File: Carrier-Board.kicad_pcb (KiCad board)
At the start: 4 copper layers, 92 x 96 mm, 54 parts, among them J1 CONN_3-6318491-6, J10 Conn_02x03_Odd_Even, J2 Conn_01x0, J4 SI-51009-F, J6 Conn_01x03_Male, J7 Conn_01x03_Male, J8 Conn_01x06_Male, J9 Conn_02x04_Odd_Even, SW1 SW_Push, SW2 SW_Push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

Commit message: PLACED STUFF
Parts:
- J10, J2, J4, J6, J7, J8, J9: moved to B.Cu
- moved J9 175.3 mm to (103.6, 115.2), turned to 270 degrees
- moved R32 166.5 mm to (91.9, 64.2), turned to 270 degrees
- moved U9 162.8 mm to (99.3, 87.1), turned to 90 degrees
- moved C29 162.0 mm to (98.8, 84.6), turned to 180 degrees
- moved J7 158.1 mm to (125.9, 115.1), turned to 270 degrees
- moved C28 154.0 mm to (99.4, 72.3), turned to 180 degrees
- moved C27 151.8 mm to (99.4, 65.6), turned to 0 degrees
- moved J8 150.5 mm to (135.0, 115.1), turned to 270 degrees
- moved R11 132.2 mm to (170.3, 104.0), turned to 0 degrees
- moved SW1 130.7 mm to (171.1, 103.8), turned to 180 degrees
- moved J10 129.5 mm to (152.6, 115.4), turned to 270 degrees
- moved R12 127.8 mm to (168.5, 97.8), turned to 0 degrees
- moved SW2 125.1 mm to (171.0, 99.0), turned to 180 degrees
- moved R13 123.8 mm to (168.5, 94.1), turned to 0 degrees
- moved SW3 119.7 mm to (171.0, 94.2), turned to 180 degrees
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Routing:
- net mCOM_5V_SBY: track 51.8 -> 25.6 mm, vias 2 -> 1
- net GBE0_CTREF(GND): track 84.5 -> 67.4 mm, vias 20 -> 19
- net mCOM_12V: track 84.4 -> 68.3 mm, vias 2 -> 1
- net +3.3V: track 78.3 -> 64.5 mm
- net Net-(D5-Pad2): track 2.44 -> 0.04 mm, vias 1 -> 0
- net Net-(D8-Pad1): vias 1 -> 0
- net Net-(D7-Pad1): vias 1 -> 0
- net Net-(D6-Pad1): vias 1 -> 0

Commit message: stuff
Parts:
- D6, D7, D8, SW1, SW2, SW3: moved to B.Cu
- R11, R12, R13, R23, R24, R25, R32: moved to F.Cu
- moved J4 100.5 mm to (78.7, 80.0), turned to 90 degrees
- moved m2 87.2 mm to (93.6, 94.8), turned to 0 degrees
- moved m1 85.9 mm to (169.3, 94.8), turned to 0 degrees
- moved m1 52.1 mm to (93.6, 47.9), turned to 0 degrees
- moved R32 50.4 mm to (136.8, 41.3), turned to 180 degrees
- moved R9 47.6 mm to (107.0, 67.1)
- moved R10 43.6 mm to (107.1, 77.4)
- moved U9 41.0 mm to (113.9, 48.7), turned to 0 degrees
- moved C29 40.4 mm to (116.4, 48.2), turned to 90 degrees
- moved C27 39.6 mm to (135.4, 48.9), turned to 270 degrees
- moved C28 37.5 mm to (128.6, 48.8), turned to 90 degrees
- moved G1 34.3 mm to (128.1, 108.2), turned to 0 degrees
- moved R25 32.0 mm to (169.8, 72.0)
- moved D8 31.9 mm to (169.1, 72.0)
- moved G1 30.0 mm to (150.4, 66.3), turned to 270 degrees
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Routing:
- net mCOM_5V_SBY: track 25.6 -> 12.4 mm, vias 1 -> 0
- net (no net): track 0.00 -> 11.5 mm, vias 0 -> 1
- net +3.3V: track 64.5 -> 70.3 mm
- net GBE0_CTREF(GND): track 67.4 -> 61.6 mm
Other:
- board text added: "S/N: 0C137-A"
- board text removed: "S/N: 0C137"

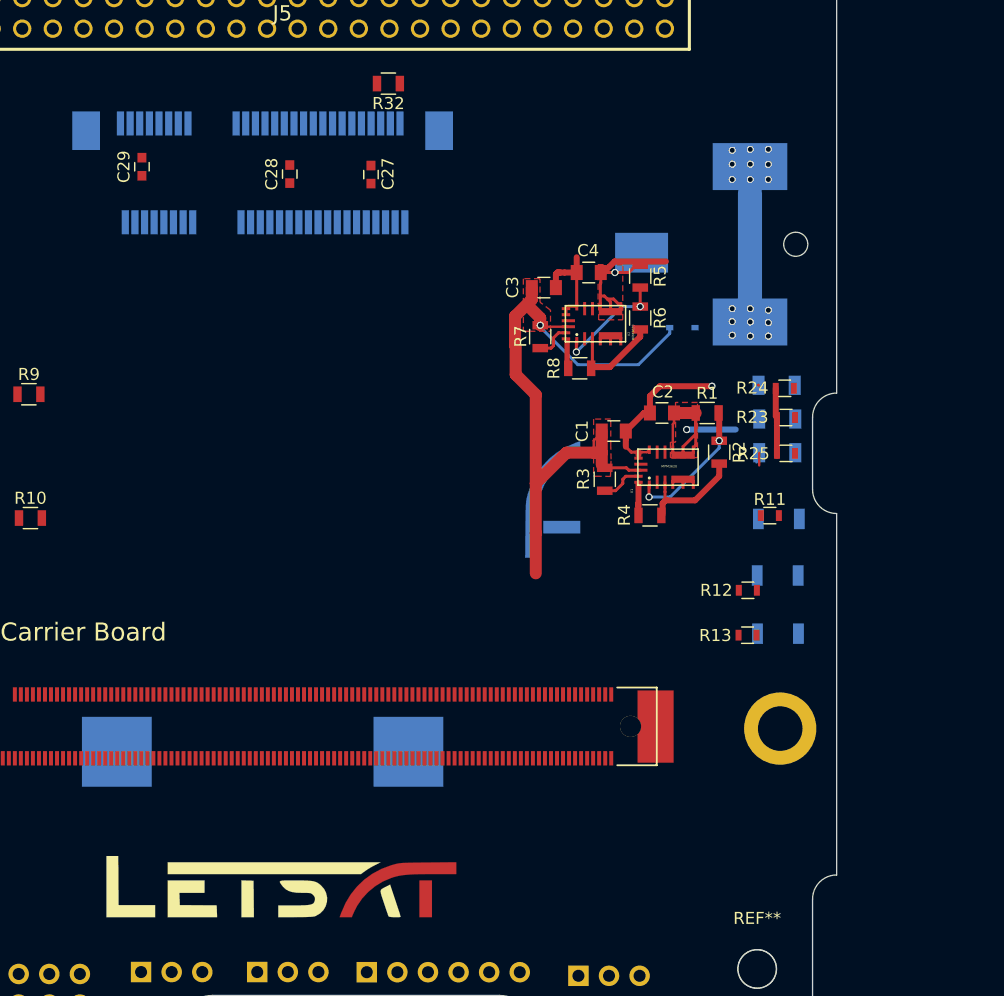
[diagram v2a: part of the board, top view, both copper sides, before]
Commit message: Make room for more screws
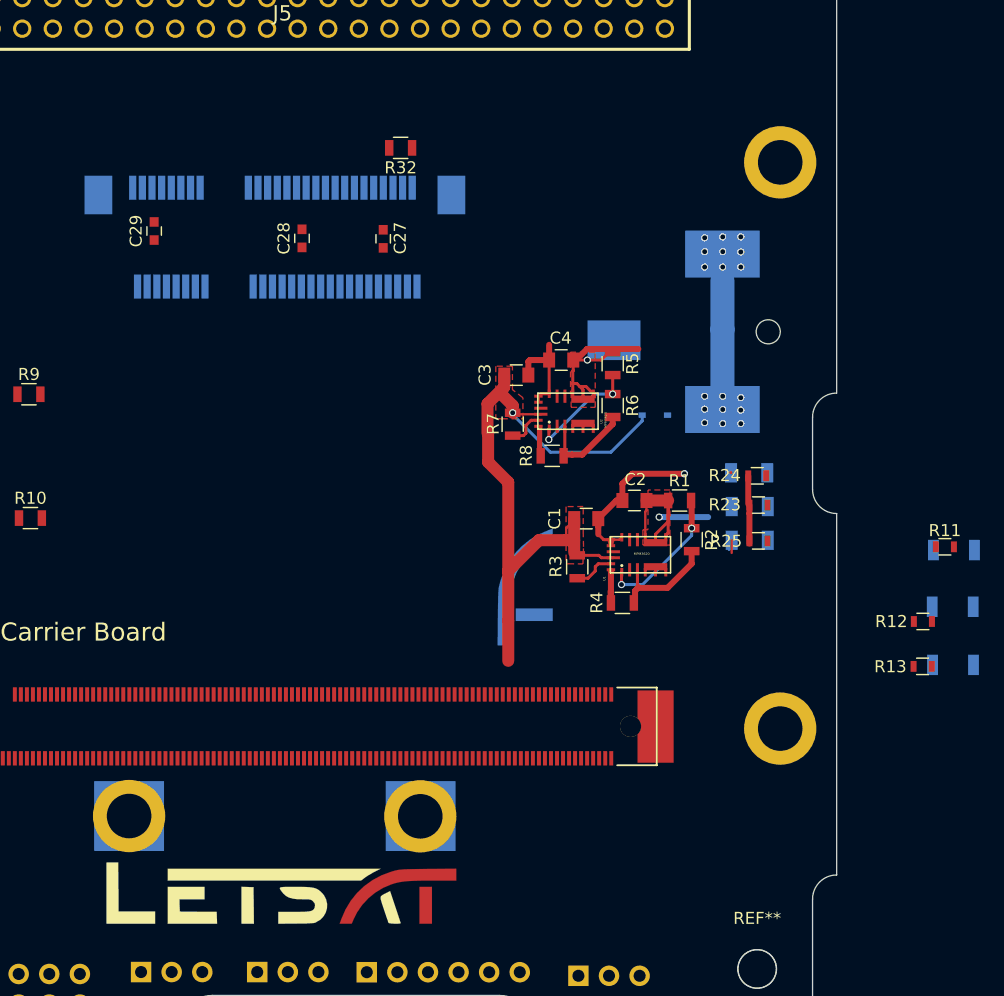
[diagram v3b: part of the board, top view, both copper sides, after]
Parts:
- added m1: MountingHole_2.7mm_M2.5_Pad, Mounting_Holes:MountingHole_2.7mm_M2.5_Pad, F.Cu at (115.3, 102.1)
- added m1: MountingHole_2.7mm_M2.5_Pad, Mounting_Holes:MountingHole_2.7mm_M2.5_Pad, F.Cu at (139.5, 102.1)
- added m2: MountingHole_2.7mm_M2.5_Pad, Mounting_Holes:MountingHole_2.7mm_M2.5_Pad, F.Cu at (169.3, 47.9)
- moved R11 14.8 mm to (183.0, 79.8)
- moved SW1 14.8 mm to (183.8, 80.0)
- moved R12 14.8 mm to (181.2, 86.0)
- moved R13 14.8 mm to (181.2, 89.7)
- moved SW2 14.8 mm to (183.7, 84.7)
- moved SW3 14.8 mm to (183.7, 89.6)
- moved G1 7.62 mm to (148.1, 73.6)
- moved R25 7.62 mm to (167.5, 79.3)
- moved R8 7.62 mm to (150.4, 72.2)
- moved C3 7.62 mm to (147.4, 65.5)
- moved C4 7.62 mm to (151.2, 64.3)
- moved D5 7.62 mm to (158.9, 68.8)
- moved J2 7.62 mm to (161.3, 61.9)
- moved R6 7.62 mm to (155.4, 68.0)
- moved R7 7.62 mm to (147.1, 69.6)
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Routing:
- net +3.3V: track 70.3 -> 50.5 mm
- net (no net): track 11.5 -> 23.9 mm

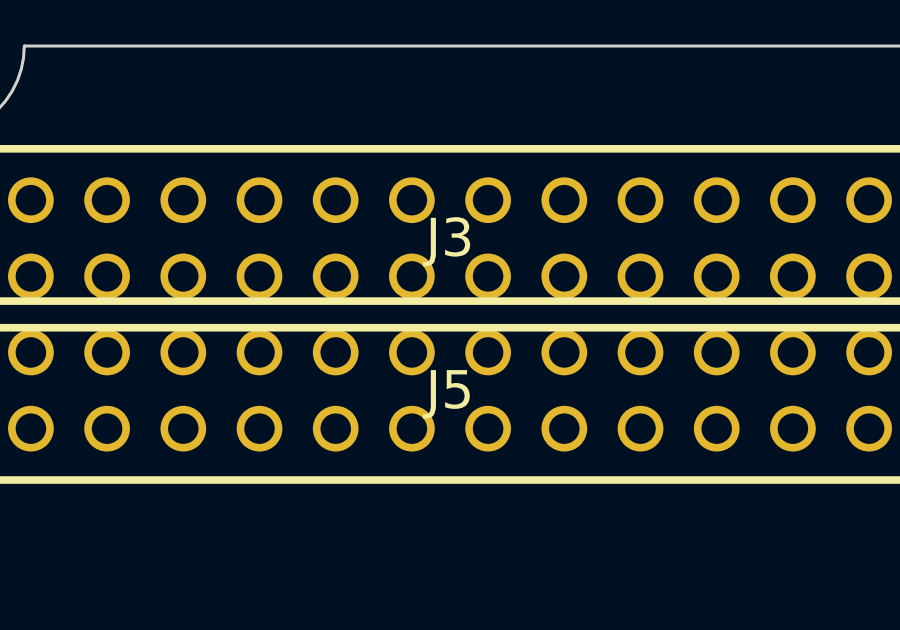
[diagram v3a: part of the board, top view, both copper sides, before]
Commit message: Rename headers
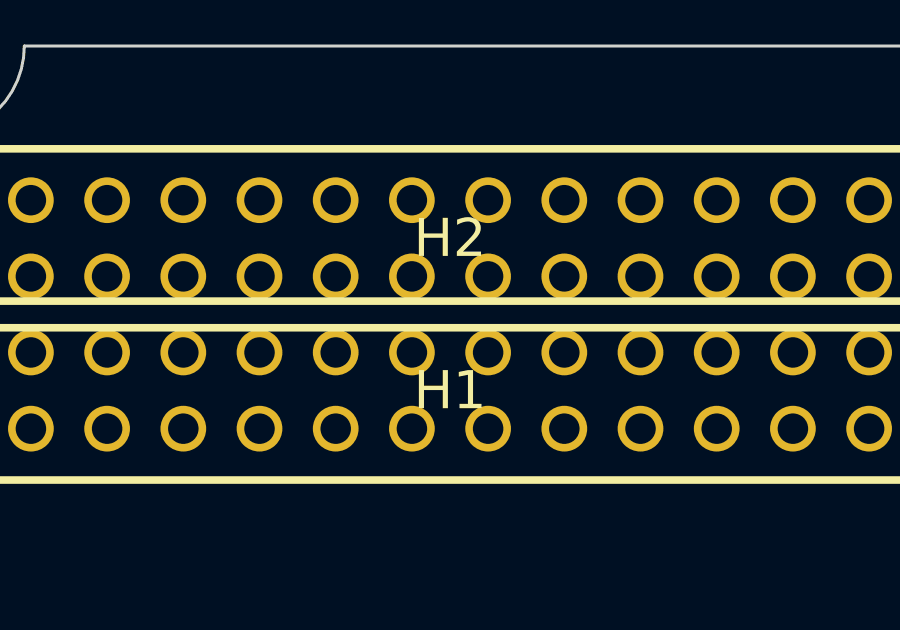
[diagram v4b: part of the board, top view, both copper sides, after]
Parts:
- renumbered J5 to H1, J3 to H2
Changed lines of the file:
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@@
     (links 180)
     (no_connects 143)
-    (area 77.857857 21.525 187.598296 130.225926)
+    (area 77.857857 21.525 187.191896 130.225926)
     (thickness 1.6)
     (drawings 7)
@@
     (tags "ELEVATED SOCKET, .100 INCH(2.54MM) PITCH")
     (attr virtual)
-    (fp_text reference J5 (at 0 0) (layer F.SilkS)
+    (fp_text reference H1 (at 0 0) (layer F.SilkS)
       (effects (font (thickness 0.15)))
     )
@@
     (tags "ELEVATED SOCKET, .100 INCH(2.54MM) PITCH")
     (attr virtual)
-    (fp_text reference J3 (at 0 0) (layer F.SilkS)
+    (fp_text reference H2 (at 0 0) (layer F.SilkS)
       (effects (font (thickness 0.15)))
     )
